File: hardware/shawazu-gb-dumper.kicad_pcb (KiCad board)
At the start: 2 copper layers, 70 x 90 mm, 16 parts, among them J1 GB_CART, SW1 VSEL, U1 BOB-12009, U2 BOB-12009, U3 BOB-12009, U4 BOB-12009, U5 BOB-12009, U6 BOB-12009, U7 BOB-12009, U8 Pico

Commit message: switched TP nCS with CLK
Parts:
- TP2: value PICO_~{CS} -> PICO_CLK
- moved TP2 1.00 mm to (114.5, 78.0)
- renumbered 10KΩ to R1
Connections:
- JP1 pad 2: pico_~{CS} -> pico_CLK
- TP2 pad 1: pico_~{CS} -> pico_CLK
- U8 pad 34: pico_CLK -> pico_~{CS}
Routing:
- net pico_CLK: track 27.3 -> 23.2 mm
- net pico_~{CS}: track 35.5 -> 38.1 mm, vias 0 -> 1
- net GND: vias 49 -> 66
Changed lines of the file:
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@@
 			(size 1 0.5)
 			(layers "F.Cu" "F.Mask")
-			(net 33 "pico_~{CS}")
+			(net 42 "pico_CLK")
 			(pinfunction "B")
 			(pintype "passive")
@@
 	(footprint "TestPoint:TestPoint_Pad_D2.0mm"
 		(layer "F.Cu")
-		(at 114.5 77)
+		(at 114.5 78)
 		(descr "SMD pad as test Point, diameter 2.0mm")
 		(tags "test point SMD pad")
@@
 			)
 		)
-		(property "Value" "PICO_~{CS}"
-			(at 0 2.5 0)
+		(property "Value" "PICO_CLK"
+			(at -0.5 3 0)
 			(layer "F.SilkS")
 			(effects
@@
 			(size 2 2)
 			(layers "F.Cu" "F.Mask")
-			(net 33 "pico_~{CS}")
+			(net 42 "pico_CLK")
 			(pinfunction "1")
 			(pintype "passive")
@@
 			(layers "*.Cu" "*.Mask")
 			(remove_unused_layers no)
-			(net 42 "pico_CLK")
+			(net 33 "pico_~{CS}")
 			(pinfunction "GPIO28_ADC2")
 			(pintype "bidirectional")
@@
 			)
 			(layers "F.Cu" "F.Mask")
-			(net 42 "pico_CLK")
+			(net 33 "pico_~{CS}")
 			(pinfunction "GPIO28_ADC2")
 			(pintype "bidirectional")
@@
 		(descr "Resistor, Axial_DIN0309 series, Axial, Horizontal, pin pitch=12.7mm, 0.5W = 1/2W, length*diameter=9*3.2mm^2, http://cdn-reichelt.de/documents/datenblatt/B400/1_4W%23YAG.pdf")
 		(tags "Resistor Axial_DIN0309 series Axial Horizontal pin pitch 12.7mm 0.5W = 1/2W length 9mm diameter 3.2mm")
-		(property "Reference" "10KΩ"
+		(property "Reference" "R1"
 			(at 6.35 -2.72 -90)
 			(layer "F.SilkS")
@@
 	)
 	(via
+		(at 130 84.5)
+		(size 0.6)
+		(drill 0.3)
+		(layers "F.Cu" "B.Cu")
+		(free yes)
+		(net 31)
+	)
+	(via
+		(at 122 83.5)
+		(size 0.6)
+		(drill 0.3)
+		(layers "F.Cu" "B.Cu")
+		(free yes)
+		(net 31)
+	)
+	(via
 		(at 128 59.5)
 		(size 0.6)
@@
 	)
 	(via
+		(at 108 67)
+		(size 0.6)
+		(drill 0.3)
+		(layers "F.Cu" "B.Cu")
+		(free yes)
+		(net 31)
+	)
+	(via
 		(at 133.5 96.5)
 		(size 0.6)
@@
 	)
 	(via
+		(at 151 60.5)
+		(size 0.6)
+		(drill 0.3)
+		(layers "F.Cu" "B.Cu")
+		(free yes)
+		(net 31)
+	)
+	(via
 		(at 120 75)
 		(size 0.6)
@@
 	)
 	(via
+		(at 164.5 67.5)
+		(size 0.6)
+		(drill 0.3)
+		(layers "F.Cu" "B.Cu")
+		(free yes)
+		(net 31)
+	)
+	(via
+		(at 110.5 106)
+		(size 0.6)
+		(drill 0.3)
+		(layers "F.Cu" "B.Cu")
+		(free yes)
+		(net 31)
+	)
+	(via
 		(at 152 84.5)
 		(size 0.6)
@@
 	)
 	(via
+		(at 165 82.5)
+		(size 0.6)
+		(drill 0.3)
+		(layers "F.Cu" "B.Cu")
+		(free yes)
+		(net 31)
+	)
+	(via
 		(at 158 75.5)
 		(size 0.6)
@@
 	)
 	(via
+		(at 149.5 51.5)
+		(size 0.6)
+		(drill 0.3)
+		(layers "F.Cu" "B.Cu")
+		(free yes)
+		(net 31)
+	)
+	(via
+		(at 109.5 56)
+		(size 0.6)
+		(drill 0.3)
+		(layers "F.Cu" "B.Cu")
+		(free yes)
+		(net 31)
+	)
+	(via
 		(at 120.5 59.5)
 		(size 0.6)
@@
 	)
 	(via
+		(at 124.5 66.5)
+		(size 0.6)
+		(drill 0.3)
+		(layers "F.Cu" "B.Cu")
+		(free yes)
+		(net 31)
+	)
+	(via
 		(at 130 75.5)
 		(size 0.6)
@@
 	)
 	(via
+		(at 124 75)
+		(size 0.6)
+		(drill 0.3)
+		(layers "F.Cu" "B.Cu")
+		(free yes)
+		(net 31)
+	)
+	(via
 		(at 126 97)
 		(size 0.6)
@@
 	)
 	(via
+		(at 130.5 67)
+		(size 0.6)
+		(drill 0.3)
+		(layers "F.Cu" "B.Cu")
+		(free yes)
+		(net 31)
+	)
+	(via
 		(at 134.5 27.5)
 		(size 0.6)
@@
 	)
 	(via
+		(at 144 106)
+		(size 0.6)
+		(drill 0.3)
+		(layers "F.Cu" "B.Cu")
+		(free yes)
+		(net 31)
+	)
+	(via
 		(at 170.5 74)
 		(size 0.6)
@@
 	)
 	(via
+		(at 138 67.5)
+		(size 0.6)
+		(drill 0.3)
+		(layers "F.Cu" "B.Cu")
+		(free yes)
+		(net 31)
+	)
+	(via
 		(at 115 68.5)
 		(size 0.6)
@@
 	)
 	(via
+		(at 146.5 105.5)
+		(size 0.6)
+		(drill 0.3)
+		(layers "F.Cu" "B.Cu")
+		(free yes)
+		(net 31)
+	)
+	(via
 		(at 164.5 41)
 		(size 0.6)
@@
 	)
 	(via
+		(at 119 83.5)
+		(size 0.6)
+		(drill 0.3)
+		(layers "F.Cu" "B.Cu")
+		(free yes)
+		(net 31)
+	)
+	(via
 		(at 154 75.5)
 		(size 0.6)
@@
 	)
 	(via
+		(at 147.5 67.5)
+		(size 0.6)
+		(drill 0.3)
+		(layers "F.Cu" "B.Cu")
+		(free yes)
+		(net 31)
+	)
+	(via
 		(at 166 59.5)
 		(size 0.6)
@@
 	)
 	(segment
-		(start 119 67.5)
-		(end 135.086666 67.5)
+		(start 128 68)
+		(end 127.5 68)
 		(width 0.2)
 		(layer "F.Cu")
@@
 	)
 	(segment
-		(start 114.5 73)
-		(end 114.5 77)
+		(start 137.926666 64.66)
+		(end 135.293333 67.293333)
 		(width 0.2)
 		(layer "F.Cu")
@@
 	)
 	(segment
-		(start 137.926666 64.66)
-		(end 135.293333 67.293333)
+		(start 135.086666 67.5)
+		(end 134.586666 68)
 		(width 0.2)
 		(layer "F.Cu")
@@
 	)
 	(segment
-		(start 117.5 69)
-		(end 119 67.5)
+		(start 127.5 68)
+		(end 125 68)
 		(width 0.2)
 		(layer "F.Cu")
@@
 	)
 	(segment
-		(start 117.5 74)
-		(end 117.5 69)
+		(start 134.586666 68)
+		(end 128 68)
 		(width 0.2)
 		(layer "F.Cu")
 		(net 33)
 	)
+	(via
+		(at 125 68)
+		(size 0.6)
+		(drill 0.3)
+		(layers "F.Cu" "B.Cu")
+		(net 33)
+	)
 	(segment
-		(start 114.5 77)
-		(end 117.5 74)
+		(start 123.062 70.325394)
+		(end 123.062 89.958)
 		(width 0.2)
-		(layer "F.Cu")
+		(layer "B.Cu")
+		(net 33)
+	)
+	(segment
+		(start 123.062 70.325394)
+		(end 125 68.387394)
+		(width 0.2)
+		(layer "B.Cu")
+		(net 33)
+	)
+	(segment
+		(start 125 68.387394)
+		(end 125 68)
+		(width 0.2)
+		(layer "B.Cu")
+		(net 33)
+	)
+	(segment
+		(start 123.062 89.958)
+		(end 122.3 90.72)
+		(width 0.2)
+		(layer "B.Cu")
 		(net 33)
 	)
@@
 	)
 	(segment
-		(start 123.062 70.325394)
-		(end 123.062 89.958)
+		(start 117.5 74)
+		(end 117.5 70)
 		(width 0.2)
-		(layer "B.Cu")
+		(layer "F.Cu")
 		(net 42)
 	)
 	(segment
 		(start 125.226666 64.66)
-		(end 125.226666 68.160728)
+		(end 122.84 64.66)
 		(width 0.2)
-		(layer "B.Cu")
+		(layer "F.Cu")
 		(net 42)
 	)
 	(segment
-		(start 125.226666 68.160728)
-		(end 123.062 70.325394)
+		(start 114.5 77)
+		(end 114.5 78)
 		(width 0.2)
-		(layer "B.Cu")
+		(layer "F.Cu")
 		(net 42)
 	)
 	(segment
-		(start 123.062 89.958)
-		(end 122.3 90.72)
+		(start 114.5 73)
+		(end 114.5 77)
 		(width 0.2)
-		(layer "B.Cu")
+		(layer "F.Cu")
+		(net 42)
+	)
+	(segment
+		(start 122.84 64.66)
+		(end 117.5 70)
+		(width 0.2)
+		(layer "F.Cu")
+		(net 42)
+	)
+	(segment
+		(start 117.5 74)
+		(end 114.5 77)
+		(width 0.2)
+		(layer "F.Cu")
 		(net 42)
 	)

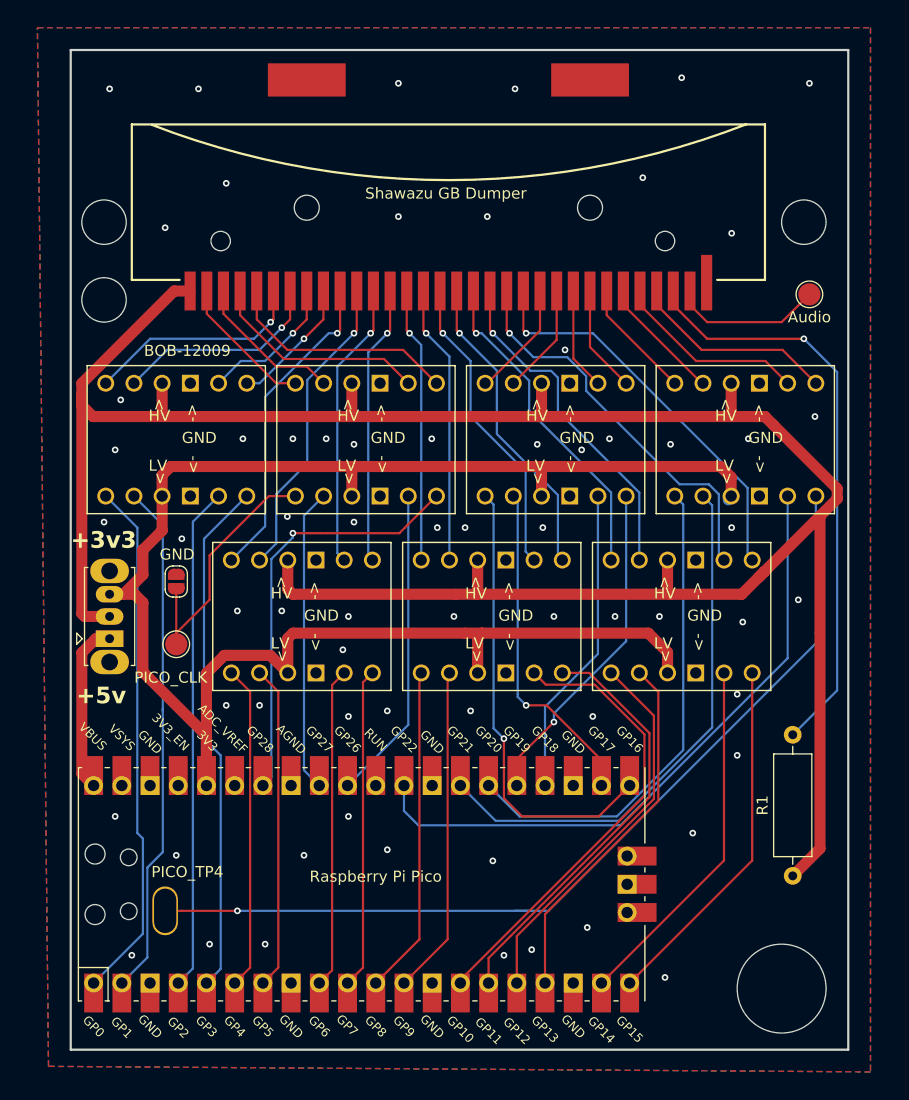
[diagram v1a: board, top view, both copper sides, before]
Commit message: removed from gnd plate
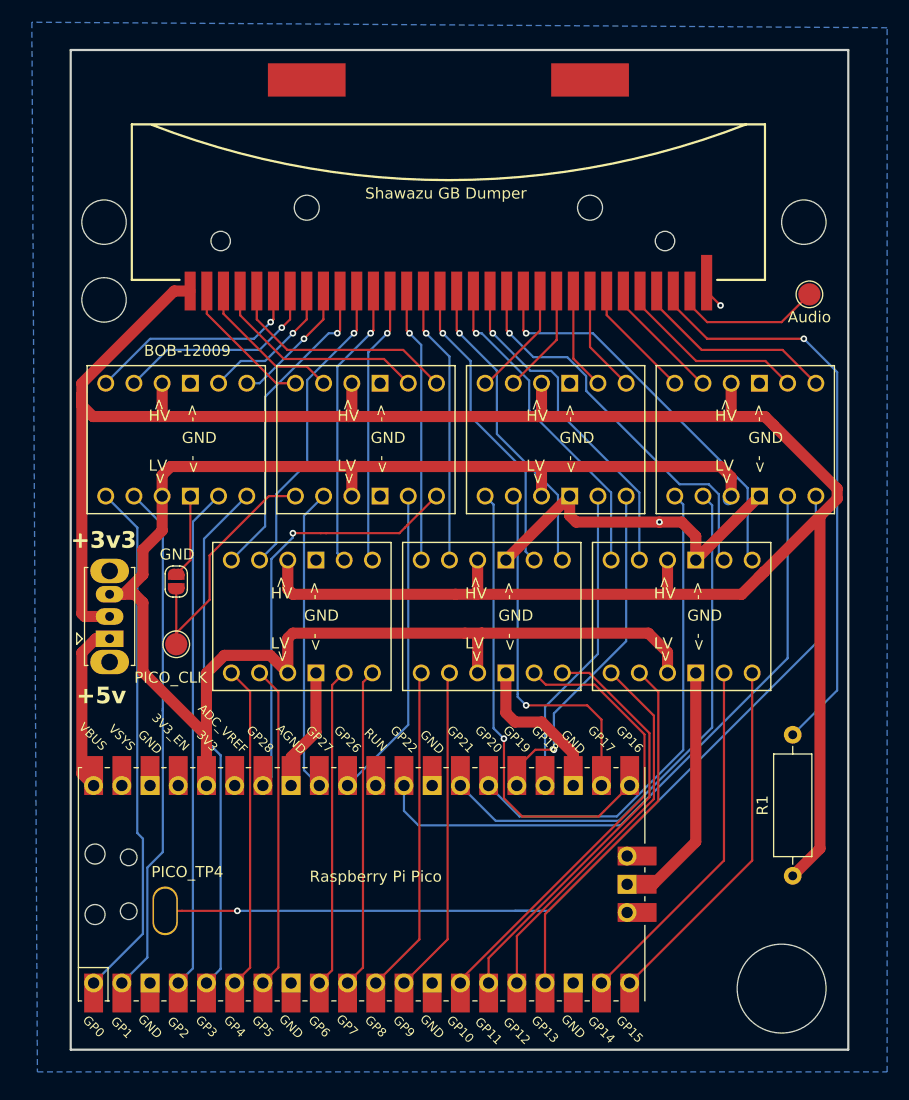
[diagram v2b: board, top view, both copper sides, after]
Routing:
- net GND: track 0.00 -> 90.5 mm, vias 66 -> 2
- net pico_D1: track 30.4 -> 32.6 mm
- net pico_D3: track 30.1 -> 31.1 mm
- removed copper zone on F.Cu, net GND

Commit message: improve gnd
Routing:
- net GND: track 90.5 -> 344.0 mm, vias 2 -> 3
